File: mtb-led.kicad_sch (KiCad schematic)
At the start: 58 parts, among them J7 AVR-ISP-6, J9 DEBUG, SW1 SW_Push, U1 ATmega328PB-A, U2 78M05, U3 TLC5940PWP, U4 TLC5940PWP, U5 MAX487E, Y1 14.7456 MHz

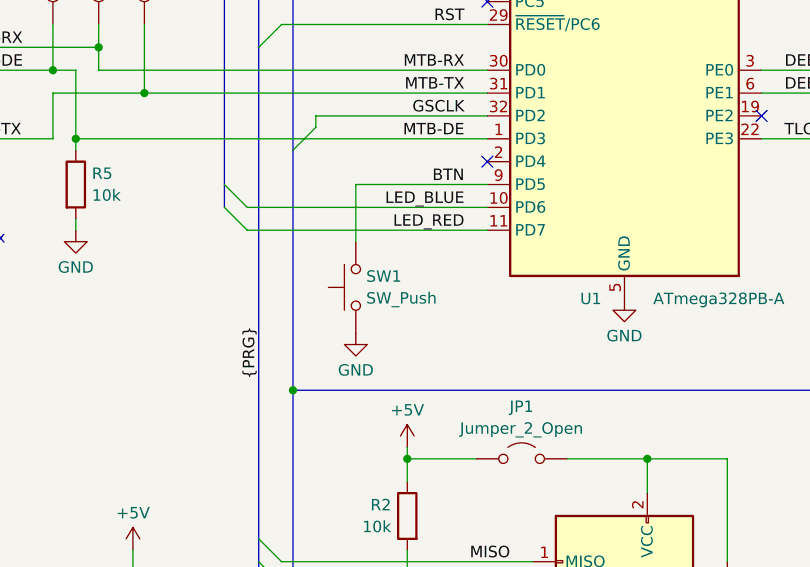
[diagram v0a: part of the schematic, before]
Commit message: Fix ERC & DRC issues.
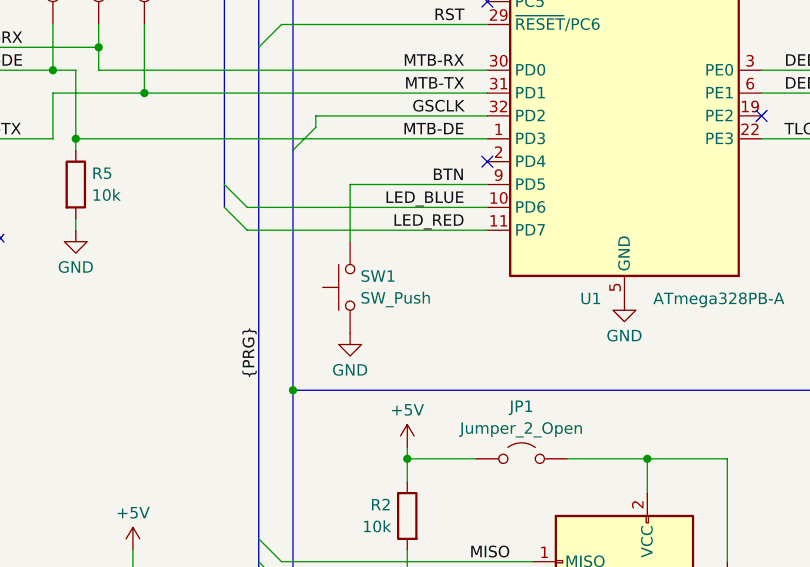
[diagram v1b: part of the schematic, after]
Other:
- moved on the sheet: SW1
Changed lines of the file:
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@@
 	(wire
 		(pts
-			(xy 208.915 100.33) (xy 208.915 106.68)
+			(xy 208.28 100.33) (xy 208.28 106.68)
 		)
 		(stroke
@@
 	(wire
 		(pts
-			(xy 208.915 100.33) (xy 223.52 100.33)
+			(xy 208.28 100.33) (xy 223.52 100.33)
 		)
 		(stroke
@@
 	(symbol
 		(lib_id "power:GND")
-		(at 208.915 116.84 0)
+		(at 208.28 116.84 0)
 		(mirror y)
 		(unit 1)
@@
 		(dnp no)
 		(property "Reference" "#PWR018"
-			(at 208.915 123.19 0)
+			(at 208.28 123.19 0)
 			(effects
 				(font
@@
 		)
 		(property "Value" "GND"
-			(at 208.915 120.9731 0)
+			(at 208.28 120.9731 0)
 			(effects
 				(font
@@
 		)
 		(property "Footprint" ""
-			(at 208.915 116.84 0)
+			(at 208.28 116.84 0)
 			(effects
 				(font
@@
 		)
 		(property "Datasheet" ""
-			(at 208.915 116.84 0)
+			(at 208.28 116.84 0)
 			(effects
 				(font
@@
 		)
 		(property "Description" "Power symbol creates a global label with name \"GND\" , ground"
-			(at 208.915 116.84 0)
+			(at 208.28 116.84 0)
 			(effects
 				(font
@@
 	(symbol
 		(lib_id "Switch:SW_Push")
-		(at 208.915 111.76 90)
+		(at 208.28 111.76 90)
 		(unit 1)
 		(exclude_from_sim no)
@@
 		(dnp no)
 		(property "Reference" "SW1"
-			(at 210.058 110.5478 90)
+			(at 209.423 110.5478 90)
 			(effects
 				(font
@@
 		)
 		(property "Value" "SW_Push"
-			(at 210.058 112.9721 90)
+			(at 209.423 112.9721 90)
 			(effects
 				(font
@@
 		)
 		(property "Footprint" "Button_Switch_THT:SW_PUSH_6mm_H4.3mm"
-			(at 203.835 111.76 0)
+			(at 203.2 111.76 0)
 			(effects
 				(font
@@
 		)
 		(property "Datasheet" "~"
-			(at 203.835 111.76 0)
+			(at 203.2 111.76 0)
 			(effects
 				(font
@@
 		)
 		(property "Description" "Push button switch, generic, two pins"
-			(at 208.915 111.76 0)
+			(at 208.28 111.76 0)
 			(effects
 				(font
@@
 		)
 		(property "JLCPCB_IGNORE" "true"
-			(at 208.915 111.76 90)
+			(at 208.28 111.76 90)
 			(effects
 				(font
